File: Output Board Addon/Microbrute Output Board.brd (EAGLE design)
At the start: 15.9 x 25.7 mm, 28 parts, among them U1 TL074_SMD

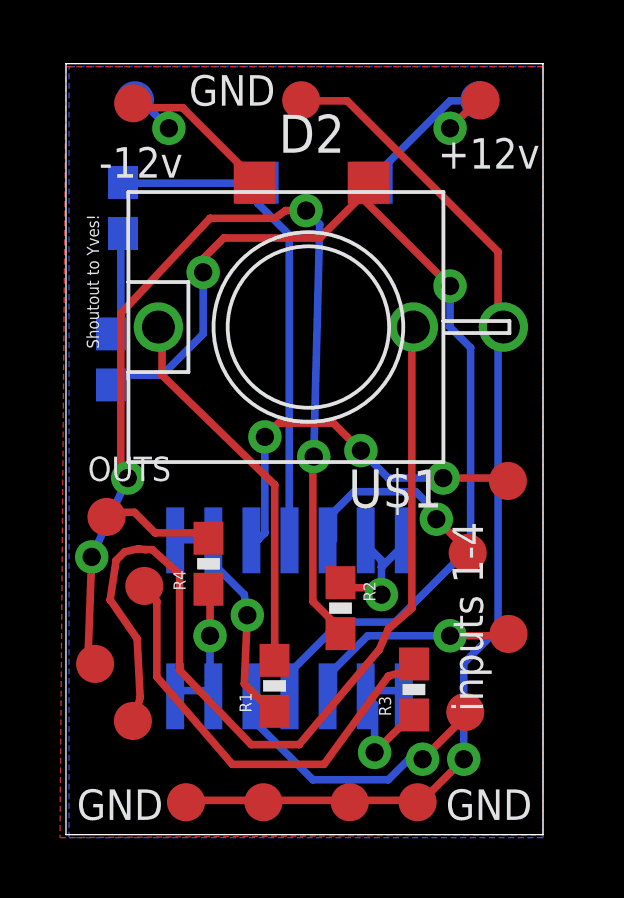
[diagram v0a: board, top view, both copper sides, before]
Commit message: Fixed vital problem: Orientation of power diodes was wrong
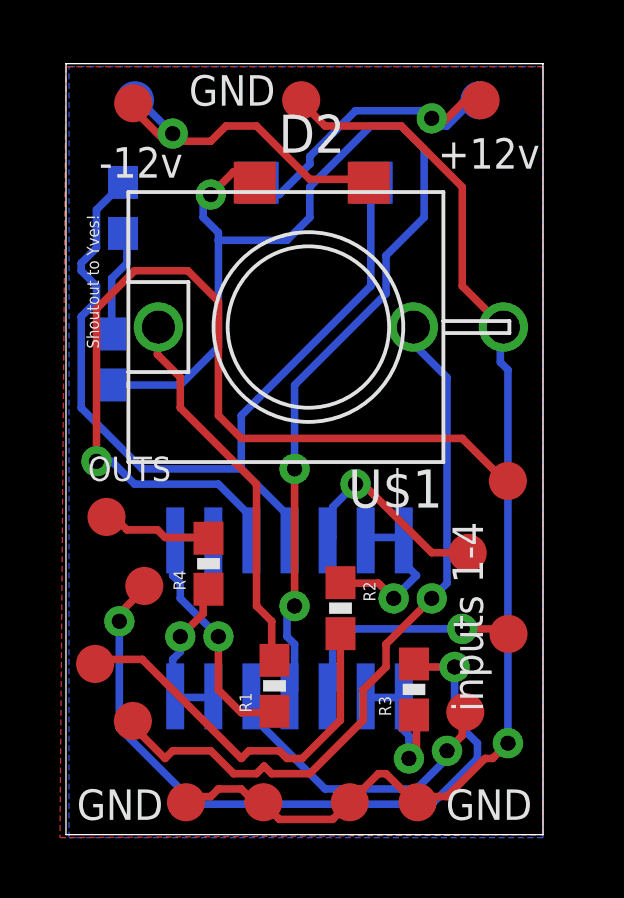
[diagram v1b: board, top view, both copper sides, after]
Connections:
- net N$1: now also D1.C; no longer D1.A
- net N$2: now also D2.A; no longer D2.C
- net VCC: now also D1.A; no longer D1.C
- net VEE: now also D2.C; no longer D2.A
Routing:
- net N$5: track 34.4 -> 13.3 mm, vias 4 -> 0
- net N$15: track 12.8 -> 31.1 mm, vias 3 -> 1
- net VCC: track 16.8 -> 29.1 mm
- net N$10: track 15.5 -> 23.6 mm, vias 0 -> 2
- net N$4: track 31.9 -> 24.4 mm, vias 0 -> 1
- net VEE: track 35.5 -> 41.1 mm, vias 2 -> 3
- net N$1: track 6.82 -> 11.5 mm
- net N$2: track 7.43 -> 11.4 mm
- net GND: track 36.2 -> 39.9 mm
- net N$8: track 7.87 -> 9.17 mm
- net N$9: track 4.71 -> 5.80 mm
- net N$13: track 7.28 -> 8.02 mm
- net N$14: track 9.82 -> 10.5 mm
